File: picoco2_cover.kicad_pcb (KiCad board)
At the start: 2 copper layers, 54 x 102.9 mm, 40 parts, among them J1 Conn_01x03_Female, J2 Micro_SD_Card, J3 Conn_01x03_Female, Q1 Q_NMOS_GDS, SW1 SW_Push, SW2 SW_Push, U1 PicoW, U2 scd30, U3 ssd1306, U4 PCF8523T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

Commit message: avoided copper keepouts
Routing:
- net SDA: track 197.1 -> 190.5 mm, vias 14 -> 10
- net VSYS: track 50.4 -> 52.4 mm, vias 4 -> 6
- net SCL: track 164.0 -> 165.4 mm, vias 6 -> 8
- net VBAT_AAA: track 91.3 -> 90.3 mm

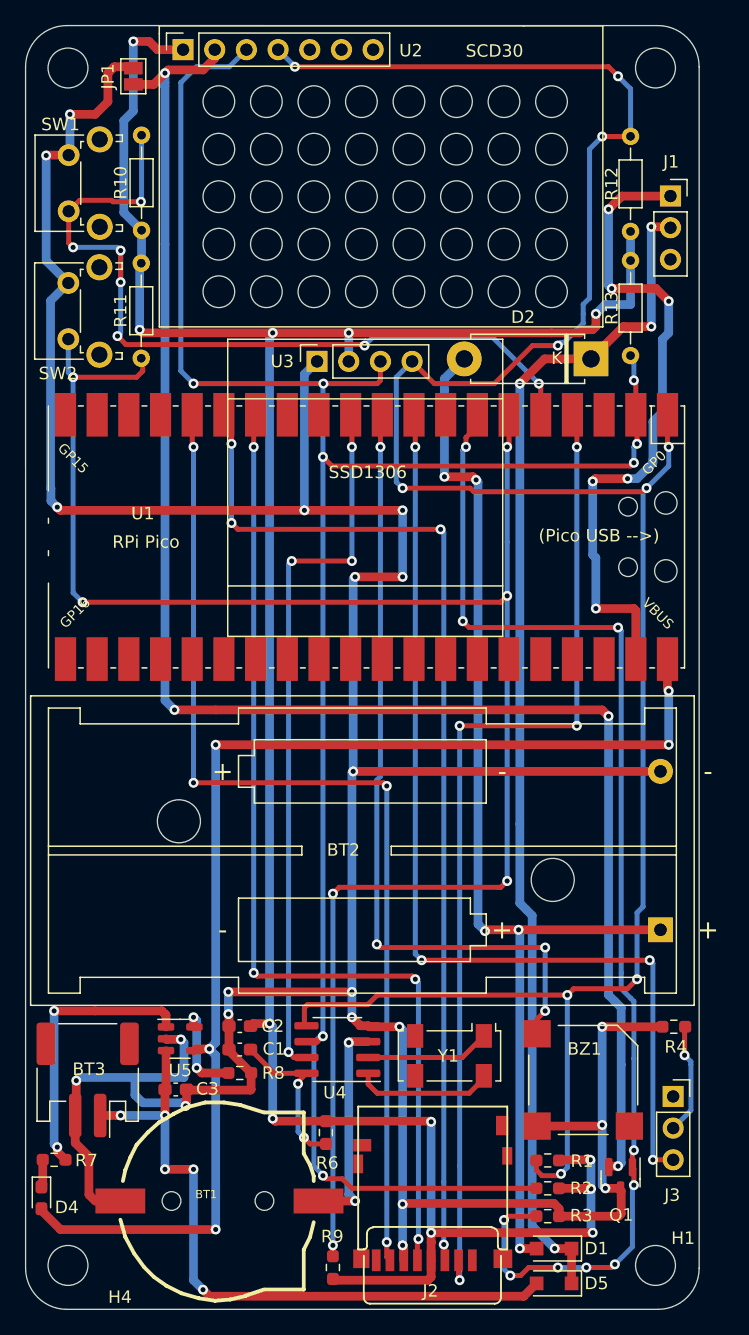
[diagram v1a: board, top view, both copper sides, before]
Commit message: recentered the display
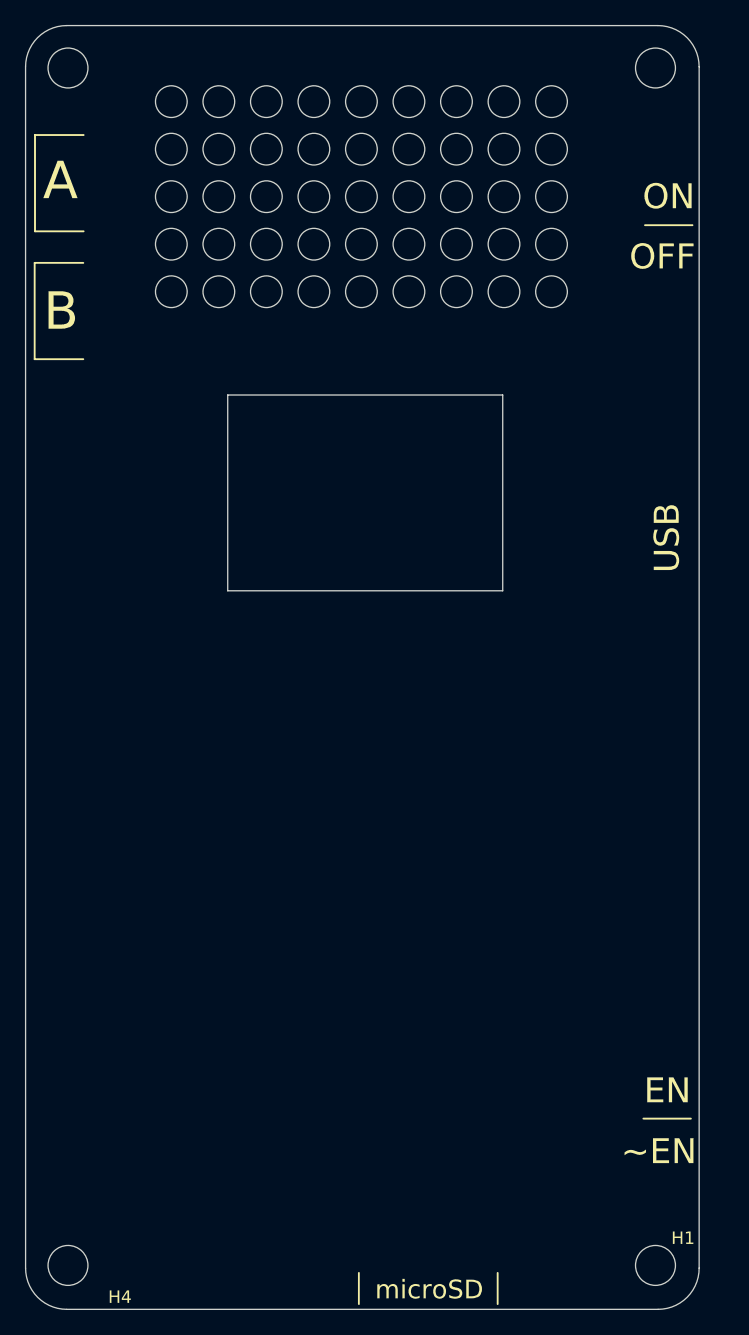
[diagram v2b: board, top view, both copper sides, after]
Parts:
- removed BT1: Battery, picoco2:CR1220-2
- removed BT2: Battery, Battery:BatteryHolder_Keystone_2468_2xAAA
- removed BT3: Battery, Connector_JST:JST_PH_S2B-PH-SM4-TB_1x02-1MP_P2.00mm_Horizontal
- removed BZ1: Buzzer, Buzzer_Beeper:MagneticBuzzer_Kobitone_254-EMB84Q-RO
- removed C1, C2, C3: C, Capacitor_SMD:C_0603_1608Metric_Pad1.08x0.95mm_HandSolder
- removed D1, D5: D, Diode_SMD:D_SOD-123F
- removed D2: D, Diode_THT:D_5W_P10.16mm_Horizontal
- removed D4: LED, LED_SMD:LED_0603_1608Metric_Pad1.05x0.95mm_HandSolder
- removed J1, J3: Conn_01x03_Female, Connector_PinSocket_2.54mm:PinSocket_1x03_P2.54mm_Vertical
- removed J2: Micro_SD_Card, picoco2:DM3D-SF_outline
- removed JP1: SolderJumper_2_Open, Jumper:SolderJumper-2_P1.3mm_Open_Pad1.0x1.5mm
- removed Q1: Q_NMOS_GDS, Package_TO_SOT_SMD:SOT-23
- removed R1, R2, R3, R4, R6, R9: R, Resistor_SMD:R_0603_1608Metric_Pad0.98x0.95mm_HandSolder
- removed R10, R11, R12, R13: R, Resistor_THT:R_Axial_DIN0204_L3.6mm_D1.6mm_P7.62mm_Horizontal
- removed R7: 1K, Resistor_SMD:R_0603_1608Metric_Pad0.98x0.95mm_HandSolder
- removed R8: 10K, Resistor_SMD:R_0603_1608Metric_Pad0.98x0.95mm_HandSolder
- removed SW1, SW2: SW_Push, Button_Switch_THT:SW_Tactile_SPST_Angled_PTS645Vx31-2LFS
- removed U1: PicoW, RPi_Pico:RPi_PicoW_SMD
- removed U2: scd30, picoco2:scd30_a
- removed U3: ssd1306, picoco2:ssd1306_a
- removed U4: PCF8523T, Package_SO:SOIC-8_3.9x4.9mm_P1.27mm
- removed U5: MCP73831-2-OT, Package_TO_SOT_SMD:SOT-23-5
- removed Y1: Crystal_GND23, Crystal:Crystal_SMD_Abracon_ABS25-4Pin_8.0x3.8mm
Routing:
- net GND: track 276.5 -> 0.00 mm, vias 21 -> 0
- net +3V3: track 200.2 -> 0.00 mm, vias 12 -> 0
- net SDA: track 190.5 -> 0.00 mm, vias 10 -> 0
- net SCL: track 165.4 -> 0.00 mm, vias 8 -> 0
- net BUT_B: track 142.7 -> 0.00 mm, vias 7 -> 0
- net SCD30_GND: track 132.4 -> 0.00 mm, vias 4 -> 0
- net VBUS: track 99.4 -> 0.00 mm, vias 5 -> 0
- net SCD30_EN: track 97.2 -> 0.00 mm, vias 10 -> 0
- net Net-(D1-Pad1): track 96.7 -> 0.00 mm, vias 4 -> 0
- net VBAT_AAA: track 90.3 -> 0.00 mm, vias 5 -> 0
- net MOSI: track 83.7 -> 0.00 mm, vias 4 -> 0
- net MISO: track 82.4 -> 0.00 mm, vias 4 -> 0
- net SCK: track 79.7 -> 0.00 mm, vias 4 -> 0
- net SD_CS: track 79.7 -> 0.00 mm, vias 4 -> 0
- net WRITE_EN: track 79.1 -> 0.00 mm, vias 4 -> 0
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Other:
- outline, holes or cut-outs redrawn
- board text added: "A"
- board text added: "B"
- board text added: "EN"
- board text added: "OFF"
- board text added: "ON"
- board text added: "USB"
- board text added: "microSD"
- board text added: "~EN"
- board text removed: "(Pico USB -->)"
- board text removed: "RPi Pico"
- board text removed: "SCD30"
- board text removed: "SSD1306"
